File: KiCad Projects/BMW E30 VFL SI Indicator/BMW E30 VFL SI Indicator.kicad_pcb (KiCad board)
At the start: 2 copper layers, 58 x 32.4 mm, 13 parts, among them J1 Conn_01x13_Socket

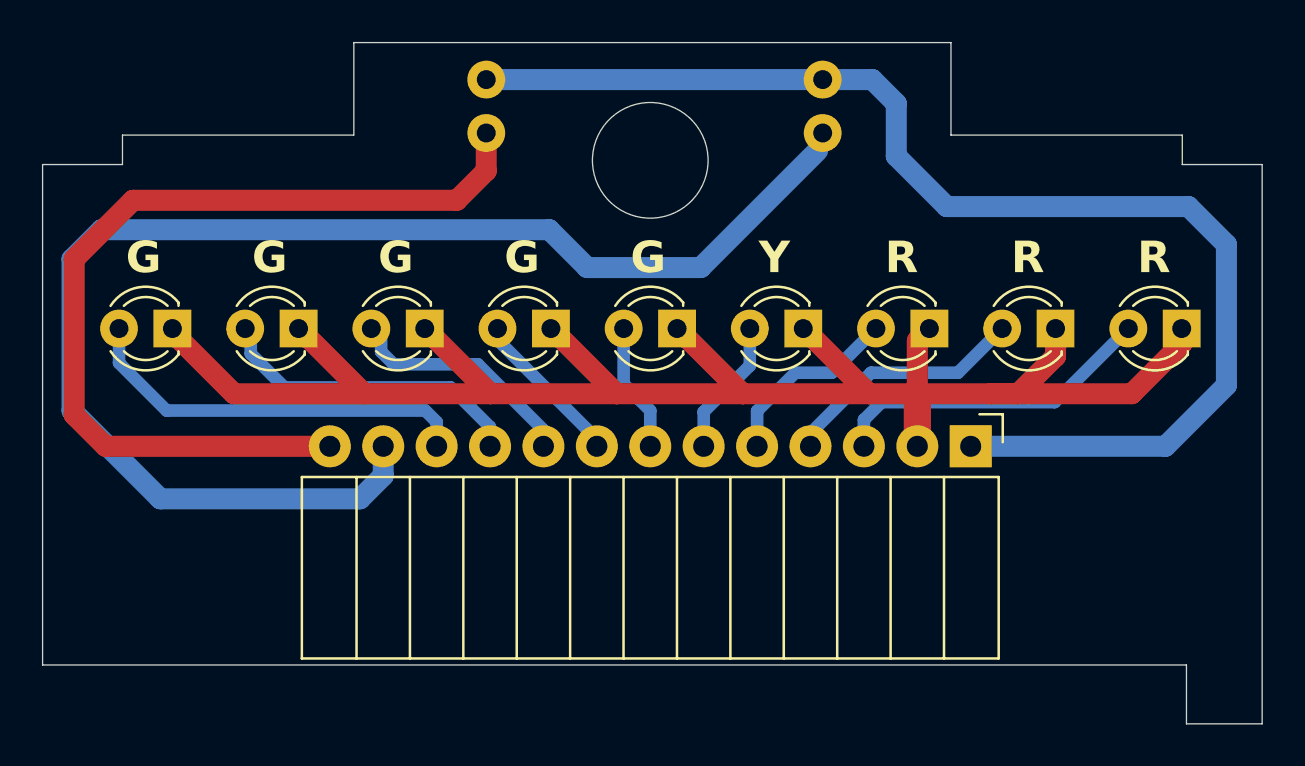
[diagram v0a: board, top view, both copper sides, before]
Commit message: Moved connectur up 2.5mm to correct board fitment
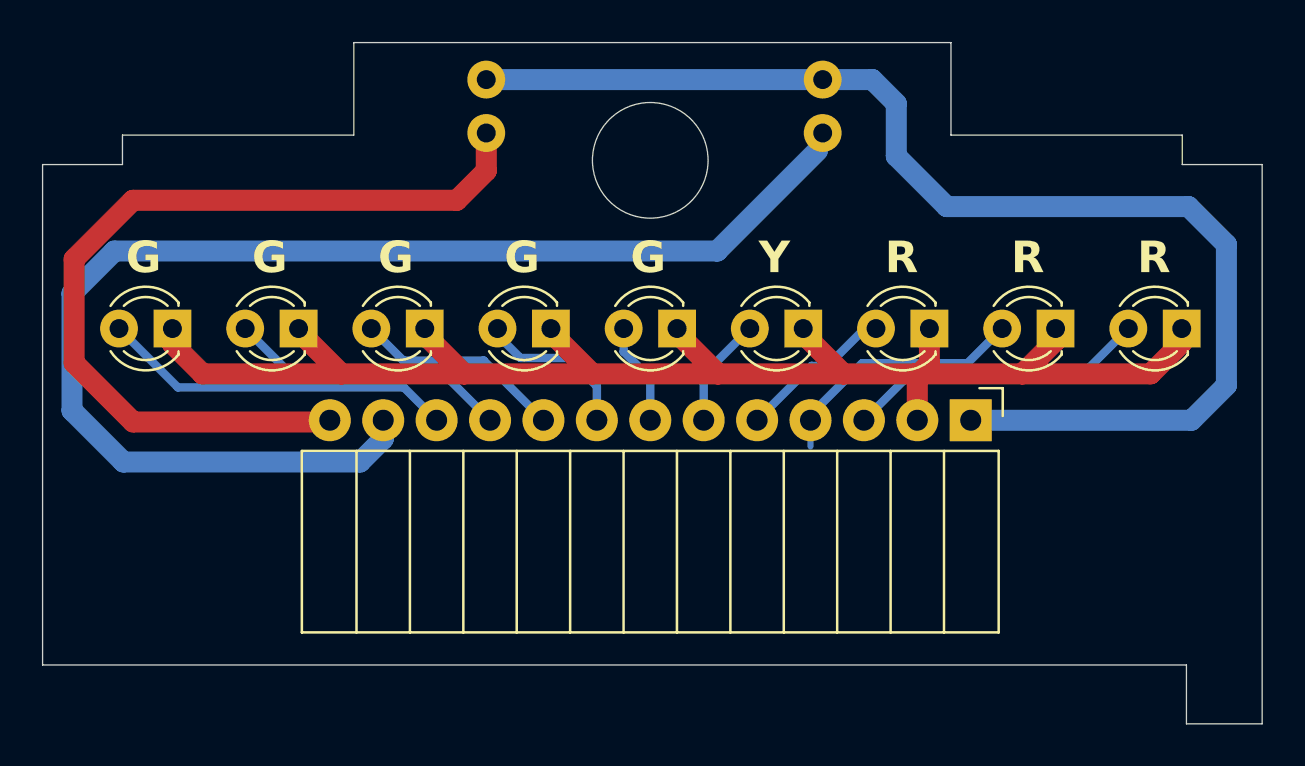
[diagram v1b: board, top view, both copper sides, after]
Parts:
- moved J1 1.24 mm to (135.1, 90.4)
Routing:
- net Net-(D1-K): track 84.1 -> 73.1 mm
- net Net-(J1-BULB_INSPECTION): track 64.7 -> 61.0 mm
- net Net-(D9-A): track 19.1 -> 16.9 mm
- net Net-(J1-BULB_OILSERVICE): track 43.3 -> 41.4 mm
- net Net-(D8-A): track 15.1 -> 13.5 mm
- net Net-(D3-A): track 8.96 -> 7.46 mm
- net Net-(D7-A): track 11.3 -> 9.99 mm
- net Net-(D1-A): track 15.6 -> 14.4 mm
- net Net-(D5-A): track 6.12 -> 4.88 mm
- net Net-(D4-A): track 6.51 -> 5.27 mm
- net Net-(J1-GND_BULB): track 60.0 -> 59.5 mm
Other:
- board text added: "F. GMEINER 05/24 V2.0"
- board text removed: "F. GMEINER 05/24 V1.0"
